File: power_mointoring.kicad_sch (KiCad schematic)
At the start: 17 parts, among them J10 BATT out, J7 VCC, J8 Servo pwr, J9 BATT in, SW5 POWER, U3 3V3 REG, U4 DS2438Z+, U5 DS2438Z+

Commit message: Ready for fab.
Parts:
- added TP1: ONEWIRE_BUS, TestPoint:TestPoint_Pad_D2.0mm, symbol Connector:TestPoint
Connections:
- net ONEWIRE_BUS: now also TP1.1
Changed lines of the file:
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@@
   (junction (at 149.86 72.39) (diameter 0) (color 0 0 0 0)
   )
+  (junction (at 194.31 116.84) (diameter 0) (color 0 0 0 0)
+  )
   (junction (at 77.47 43.18) (diameter 0) (color 0 0 0 0)
   )
@@
     (stroke (width 0) (type default) (color 0 0 0 0))
   )
+  (wire (pts (xy 194.31 116.84) (xy 199.39 116.84))
+    (stroke (width 0) (type default) (color 0 0 0 0))
+  )
   (wire (pts (xy 53.34 114.3) (xy 58.42 114.3))
     (stroke (width 0) (type default) (color 0 0 0 0))
@@
     (stroke (width 0) (type default) (color 0 0 0 0))
   )
+  (wire (pts (xy 194.31 109.22) (xy 194.31 116.84))
+    (stroke (width 0) (type default) (color 0 0 0 0))
+  )
   (wire (pts (xy 99.06 119.38) (xy 104.14 119.38))
     (stroke (width 0) (type default) (color 0 0 0 0))
@@
     (stroke (width 0) (type default) (color 0 0 0 0))
   )
-  (wire (pts (xy 189.23 116.84) (xy 199.39 116.84))
+  (wire (pts (xy 189.23 116.84) (xy 194.31 116.84))
     (stroke (width 0) (type default) (color 0 0 0 0))
   )
@@
   (symbol (lib_id "power:+BATT") (at 104.14 119.38 0) (unit 1)
     (in_bom yes) (on_board yes)
-    (property "Reference" "#PWR066" (id 0) (at 104.14 123.19 0)
+    (property "Reference" "#PWR067" (id 0) (at 104.14 123.19 0)
       (effects (font (size 1.27 1.27)) hide)
     )
@@
   (symbol (lib_id "power:GND") (at 153.67 92.71 0) (unit 1)
     (in_bom yes) (on_board yes) (fields_autoplaced)
-    (property "Reference" "#PWR071" (id 0) (at 153.67 99.06 0)
+    (property "Reference" "#PWR072" (id 0) (at 153.67 99.06 0)
       (effects (font (size 1.27 1.27)) hide)
     )
@@
   (symbol (lib_id "power:VCC") (at 58.42 111.76 0) (unit 1)
     (in_bom yes) (on_board yes) (fields_autoplaced)
-    (property "Reference" "#PWR059" (id 0) (at 58.42 115.57 0)
+    (property "Reference" "#PWR060" (id 0) (at 58.42 115.57 0)
       (effects (font (size 1.27 1.27)) hide)
     )
@@
   (symbol (lib_id "power:GND") (at 189.23 138.43 0) (unit 1)
     (in_bom yes) (on_board yes) (fields_autoplaced)
-    (property "Reference" "#PWR074" (id 0) (at 189.23 144.78 0)
+    (property "Reference" "#PWR075" (id 0) (at 189.23 144.78 0)
       (effects (font (size 1.27 1.27)) hide)
     )
@@
   (symbol (lib_id "power:GND") (at 58.42 114.3 0) (unit 1)
     (in_bom yes) (on_board yes) (fields_autoplaced)
-    (property "Reference" "#PWR060" (id 0) (at 58.42 120.65 0)
+    (property "Reference" "#PWR061" (id 0) (at 58.42 120.65 0)
       (effects (font (size 1.27 1.27)) hide)
     )
@@
   (symbol (lib_id "power:GND") (at 189.23 76.2 0) (unit 1)
     (in_bom yes) (on_board yes) (fields_autoplaced)
-    (property "Reference" "#PWR073" (id 0) (at 189.23 82.55 0)
+    (property "Reference" "#PWR074" (id 0) (at 189.23 82.55 0)
       (effects (font (size 1.27 1.27)) hide)
     )
@@
     )
     (property "Datasheet" "" (id 3) (at 189.23 76.2 0)
+      (effects (font (size 1.27 1.27)) hide)
+    )
+    (pin "1")
+  )
+  (symbol (lib_id "Connector:TestPoint") (at 194.31 109.22 0) (unit 1)
+    (in_bom yes) (on_board yes) (fields_autoplaced)
+    (property "Reference" "TP1" (id 0) (at 196.85 104.6479 0)
+      (effects (font (size 1.27 1.27)) (justify left))
+    )
+    (property "Value" "ONEWIRE_BUS" (id 1) (at 196.85 107.1879 0)
+      (effects (font (size 1.27 1.27)) (justify left))
+    )
+    (property "Footprint" "TestPoint:TestPoint_Pad_D2.0mm" (id 2) (at 199.39 109.22 0)
+      (effects (font (size 1.27 1.27)) hide)
+    )
+    (property "Datasheet" "~" (id 3) (at 199.39 109.22 0)
       (effects (font (size 1.27 1.27)) hide)
     )
@@
   (symbol (lib_id "power:GND") (at 104.14 121.92 0) (unit 1)
     (in_bom yes) (on_board yes) (fields_autoplaced)
-    (property "Reference" "#PWR067" (id 0) (at 104.14 128.27 0)
+    (property "Reference" "#PWR068" (id 0) (at 104.14 128.27 0)
       (effects (font (size 1.27 1.27)) hide)
     )
@@
   (symbol (lib_id "power:VCC") (at 194.31 41.91 0) (unit 1)
     (in_bom yes) (on_board yes) (fields_autoplaced)
-    (property "Reference" "#PWR075" (id 0) (at 194.31 45.72 0)
+    (property "Reference" "#PWR076" (id 0) (at 194.31 45.72 0)
       (effects (font (size 1.27 1.27)) hide)
     )
@@
   (symbol (lib_id "power:VCC") (at 152.4 116.84 0) (unit 1)
     (in_bom yes) (on_board yes) (fields_autoplaced)
-    (property "Reference" "#PWR070" (id 0) (at 152.4 120.65 0)
+    (property "Reference" "#PWR071" (id 0) (at 152.4 120.65 0)
       (effects (font (size 1.27 1.27)) hide)
     )
@@
   (symbol (lib_id "power:+5V") (at 156.21 72.39 0) (unit 1)
     (in_bom yes) (on_board yes) (fields_autoplaced)
-    (property "Reference" "#PWR072" (id 0) (at 156.21 76.2 0)
+    (property "Reference" "#PWR073" (id 0) (at 156.21 76.2 0)
       (effects (font (size 1.27 1.27)) hide)
     )
@@
   (symbol (lib_id "power:+5V") (at 96.52 149.86 0) (unit 1)
     (in_bom yes) (on_board yes) (fields_autoplaced)
-    (property "Reference" "#PWR064" (id 0) (at 96.52 153.67 0)
+    (property "Reference" "#PWR065" (id 0) (at 96.52 153.67 0)
       (effects (font (size 1.27 1.27)) hide)
     )
@@
   (symbol (lib_id "power:GND") (at 64.77 46.99 0) (unit 1)
     (in_bom yes) (on_board yes) (fields_autoplaced)
-    (property "Reference" "#PWR061" (id 0) (at 64.77 53.34 0)
+    (property "Reference" "#PWR062" (id 0) (at 64.77 53.34 0)
       (effects (font (size 1.27 1.27)) hide)
     )
@@
   (symbol (lib_id "power:+BATT") (at 133.35 72.39 0) (unit 1)
     (in_bom yes) (on_board yes)
-    (property "Reference" "#PWR068" (id 0) (at 133.35 76.2 0)
+    (property "Reference" "#PWR069" (id 0) (at 133.35 76.2 0)
       (effects (font (size 1.27 1.27)) hide)
     )
@@
   (symbol (lib_id "power:GND") (at 101.6 154.94 0) (unit 1)
     (in_bom yes) (on_board yes) (fields_autoplaced)
-    (property "Reference" "#PWR065" (id 0) (at 101.6 161.29 0)
+    (property "Reference" "#PWR066" (id 0) (at 101.6 161.29 0)
       (effects (font (size 1.27 1.27)) hide)
     )
@@
   (symbol (lib_id "power:+BATT") (at 33.02 29.21 0) (unit 1)
     (in_bom yes) (on_board yes) (fields_autoplaced)
-    (property "Reference" "#PWR058" (id 0) (at 33.02 33.02 0)
+    (property "Reference" "#PWR059" (id 0) (at 33.02 33.02 0)
       (effects (font (size 1.27 1.27)) hide)
     )
@@
   (symbol (lib_id "power:VCC") (at 77.47 30.48 0) (unit 1)
     (in_bom yes) (on_board yes) (fields_autoplaced)
-    (property "Reference" "#PWR062" (id 0) (at 77.47 34.29 0)
+    (property "Reference" "#PWR063" (id 0) (at 77.47 34.29 0)
       (effects (font (size 1.27 1.27)) hide)
     )
@@
   (symbol (lib_id "power:+5VD") (at 144.78 116.84 0) (unit 1)
     (in_bom yes) (on_board yes) (fields_autoplaced)
-    (property "Reference" "#PWR069" (id 0) (at 144.78 120.65 0)
+    (property "Reference" "#PWR070" (id 0) (at 144.78 120.65 0)
       (effects (font (size 1.27 1.27)) hide)
     )
@@
   (symbol (lib_id "power:+5VD") (at 91.44 152.4 0) (unit 1)
     (in_bom yes) (on_board yes) (fields_autoplaced)
-    (property "Reference" "#PWR063" (id 0) (at 91.44 156.21 0)
-      (effects (font (size 1.27 1.27)) hide)
-    )
+    (property "Reference" "#PWR064" (id 0) (at 91.44 156.21 0)
+      (effects (font (size 1.27 1.27)) hide)
+    )

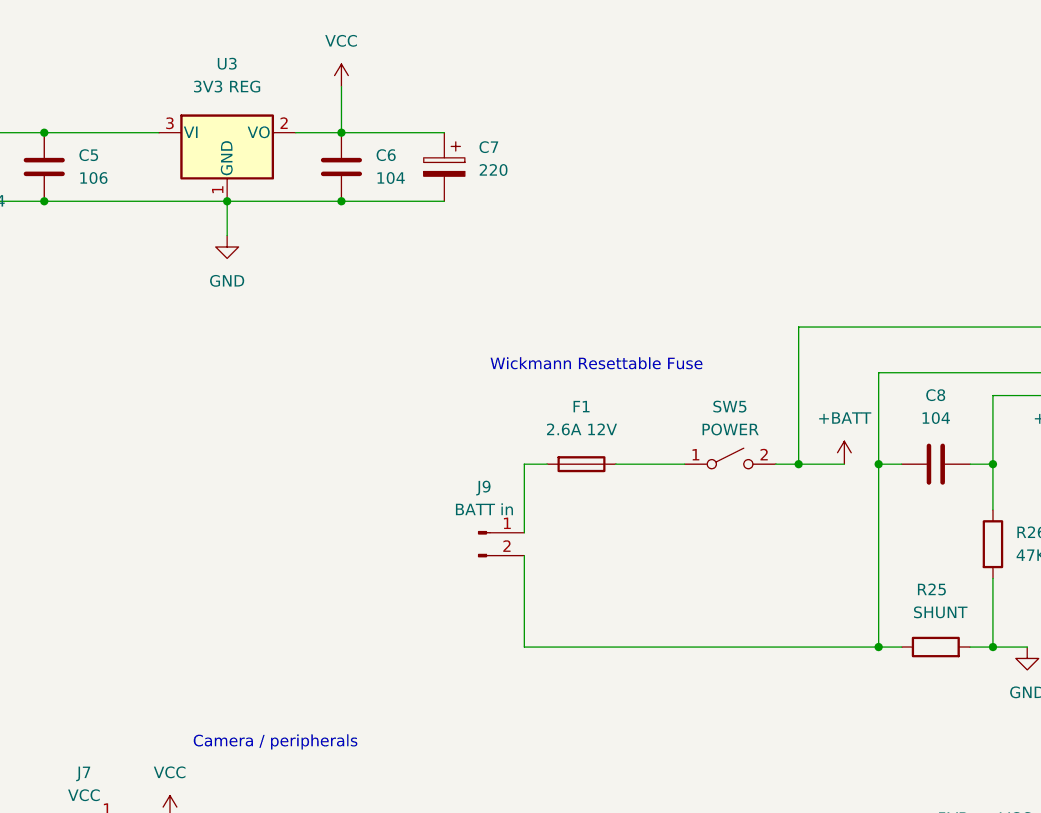
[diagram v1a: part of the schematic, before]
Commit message: Added minor footprint changes after trying to build the board. Added pin to switch battery to Vin.
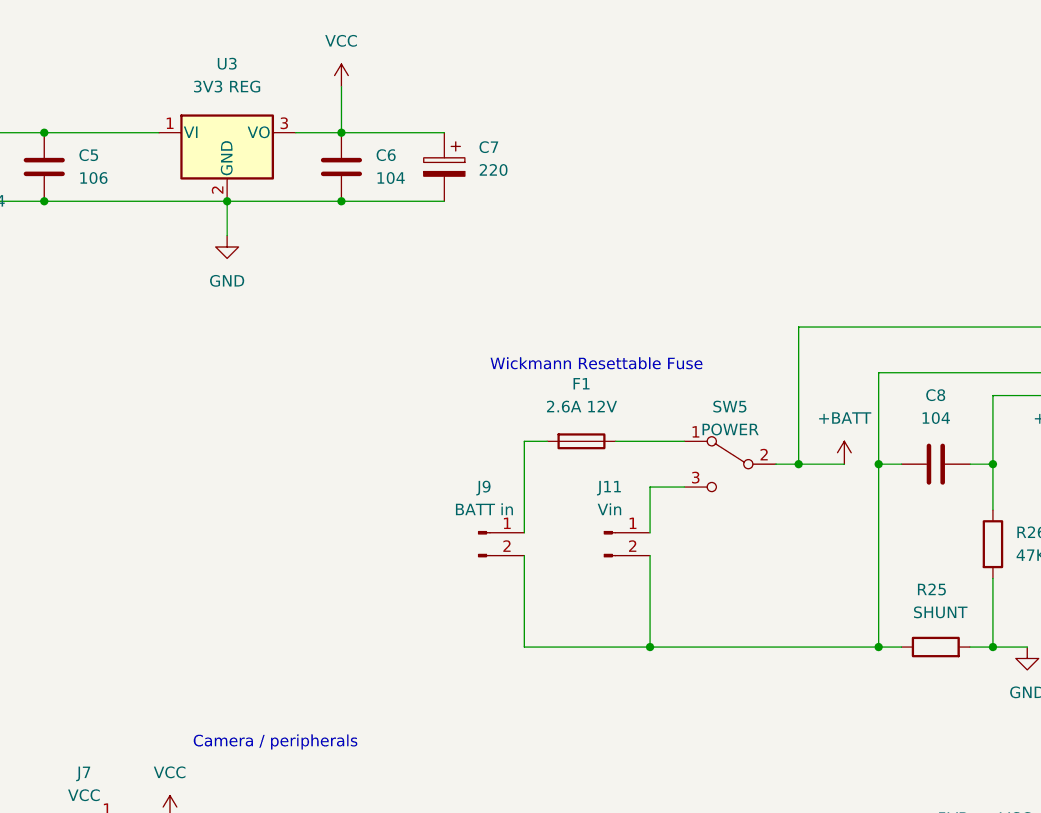
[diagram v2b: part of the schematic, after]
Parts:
- added J11: Vin, Connector_PinHeader_2.54mm:Connector_Battery_SolderPads, symbol Connector:Conn_01x02_Male
- SW5: footprint Button_Switch_THT:SW_Slide_1P2T_CK_OS102011MS2Q -> KiCAD Custom Libs:Switch-SS12F23; symbol Switch:SW_SPST -> Switch:SW_SPDT
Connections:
- net +BATT: now also U3.1 (VI); no longer U3.3 (VI)
- net GND: now also U3.2 (GND); no longer U3.1 (GND)
- net VCC: now also U3.3 (VO); no longer U3.2 (VO)
- net at C8.2, J9.2 (Pin_2), R25.1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: now also J11.2 (Pin_2)
- new net: J11.1 (Pin_1), SW5.3 (C)
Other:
- moved on the sheet: F1
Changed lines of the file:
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@@
     (company "James Hudson")
   )
+  (junction (at 111.76 92.71) (diameter 0) (color 0 0 0 0)
+  )
   (junction (at 128.27 72.39) (diameter 0) (color 0 0 0 0)
   )
@@
     (stroke (width 0) (type default) (color 0 0 0 0))
   )
+  (wire (pts (xy 111.76 80.01) (xy 111.76 74.93))
+    (stroke (width 0) (type default) (color 0 0 0 0))
+  )
   (wire (pts (xy 99.06 121.92) (xy 104.14 121.92))
     (stroke (width 0) (type default) (color 0 0 0 0))
@@
     (stroke (width 0) (type default) (color 0 0 0 0))
   )
+  (wire (pts (xy 111.76 74.93) (xy 115.57 74.93))
+    (stroke (width 0) (type default) (color 0 0 0 0))
+  )
   (wire (pts (xy 137.16 92.71) (xy 139.7 92.71))
     (stroke (width 0) (type default) (color 0 0 0 0))
@@
     (stroke (width 0) (type default) (color 0 0 0 0))
   )
+  (wire (pts (xy 111.76 92.71) (xy 137.16 92.71))
+    (stroke (width 0) (type default) (color 0 0 0 0))
+  )
   (wire (pts (xy 194.31 109.22) (xy 194.31 116.84))
     (stroke (width 0) (type default) (color 0 0 0 0))
@@
     (stroke (width 0) (type default) (color 0 0 0 0))
   )
+  (wire (pts (xy 111.76 82.55) (xy 111.76 92.71))
+    (stroke (width 0) (type default) (color 0 0 0 0))
+  )
   (wire (pts (xy 72.39 35.56) (xy 77.47 35.56))
     (stroke (width 0) (type default) (color 0 0 0 0))
@@
     (stroke (width 0) (type default) (color 0 0 0 0))
   )
-  (wire (pts (xy 107.95 72.39) (xy 115.57 72.39))
+  (wire (pts (xy 107.95 69.85) (xy 115.57 69.85))
     (stroke (width 0) (type default) (color 0 0 0 0))
   )
@@
     (stroke (width 0) (type default) (color 0 0 0 0))
   )
-  (wire (pts (xy 97.79 92.71) (xy 137.16 92.71))
+  (wire (pts (xy 97.79 92.71) (xy 111.76 92.71))
     (stroke (width 0) (type default) (color 0 0 0 0))
   )
@@
     (stroke (width 0) (type default) (color 0 0 0 0))
   )
-  (wire (pts (xy 97.79 72.39) (xy 100.33 72.39))
-    (stroke (width 0) (type default) (color 0 0 0 0))
-  )
-  (wire (pts (xy 97.79 72.39) (xy 97.79 80.01))
+  (wire (pts (xy 97.79 69.85) (xy 100.33 69.85))
+    (stroke (width 0) (type default) (color 0 0 0 0))
+  )
+  (wire (pts (xy 97.79 69.85) (xy 97.79 80.01))
     (stroke (width 0) (type default) (color 0 0 0 0))
   )
@@
     (pin "3")
   )
-  (symbol (lib_id "Switch:SW_SPST") (at 120.65 72.39 0) (unit 1)
+  (symbol (lib_id "Switch:SW_SPDT") (at 120.65 72.39 0) (mirror y) (unit 1)
     (in_bom yes) (on_board yes)
     (property "Reference" "SW5" (id 0) (at 120.65 66.04 0))
     (property "Value" "POWER" (id 1) (at 120.65 68.58 0))
-    (property "Footprint" "Button_Switch_THT:SW_Slide_1P2T_CK_OS102011MS2Q" (id 2) (at 120.65 72.39 0)
+    (property "Footprint" "KiCAD Custom Libs:Switch-SS12F23" (id 2) (at 120.65 72.39 0)
       (effects (font (size 1.27 1.27)) hide)
     )
     (property "Datasheet" "~" (id 3) (at 120.65 72.39 0)
+      (effects (font (size 1.27 1.27)) hide)
+    )
+    (pin "1")
+    (pin "2")
+    (pin "3")
+  )
+  (symbol (lib_id "Connector:Conn_01x02_Male") (at 106.68 80.01 0) (unit 1)
+    (in_bom yes) (on_board yes) (fields_autoplaced)
+    (property "Reference" "J11" (id 0) (at 107.315 74.93 0))
+    (property "Value" "Vin" (id 1) (at 107.315 77.47 0))
+    (property "Footprint" "Connector_PinHeader_2.54mm:Connector_Battery_SolderPads" (id 2) (at 106.68 80.01 0)
+      (effects (font (size 1.27 1.27)) hide)
+    )
+    (property "Datasheet" "~" (id 3) (at 106.68 80.01 0)
       (effects (font (size 1.27 1.27)) hide)
     )
@@
     (pin "1")
   )
-  (symbol (lib_id "Device:Fuse") (at 104.14 72.39 270) (unit 1)
-    (in_bom yes) (on_board yes) (fields_autoplaced)
-    (property "Reference" "F1" (id 0) (at 104.14 66.04 90))
-    (property "Value" "2.6A 12V" (id 1) (at 104.14 68.58 90))
-    (property "Footprint" "Fuse:Fuse_2010_5025Metric" (id 2) (at 104.14 70.612 90)
-      (effects (font (size 1.27 1.27)) hide)
-    )
-    (property "Datasheet" "~" (id 3) (at 104.14 72.39 0)
+  (symbol (lib_id "Device:Fuse") (at 104.14 69.85 270) (unit 1)
+    (in_bom yes) (on_board yes) (fields_autoplaced)
+    (property "Reference" "F1" (id 0) (at 104.14 63.5 90))
+    (property "Value" "2.6A 12V" (id 1) (at 104.14 66.04 90))
+    (property "Footprint" "Fuse:Fuse_2010_5025Metric" (id 2) (at 104.14 68.072 90)
+      (effects (font (size 1.27 1.27)) hide)
+    )
+    (property "Datasheet" "~" (id 3) (at 104.14 69.85 0)
       (effects (font (size 1.27 1.27)) hide)
     )
@@
       (effects (font (size 1.27 1.27) italic) hide)
     )
-    (property "Datasheet" "https://www.analog.com/media/en/technical-documentation/data-sheets/158457a.pdf" (id 3) (at 64.77 35.56 0)
-      (effects (font (size 1.27 1.27)) hide)
-    )
-    (pin "1")
+    (property "Datasheet" "https://www.analog.com/media/en/technical-documentation/data-sheets/158457a.pdf" (id 3) (at 64.77 57.15 0)
+      (effects (font (size 1.27 1.27)) hide)
+    )
     (pin "2")
     (pin "3")
+    (pin "1")
   )
   (symbol (lib_id "Device:C_Polarized") (at 88.9 39.37 0) (mirror y) (unit 1)
